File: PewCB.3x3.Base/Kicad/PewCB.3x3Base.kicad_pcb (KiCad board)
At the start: 2 copper layers, 53.3 x 53.3 mm, 4 parts

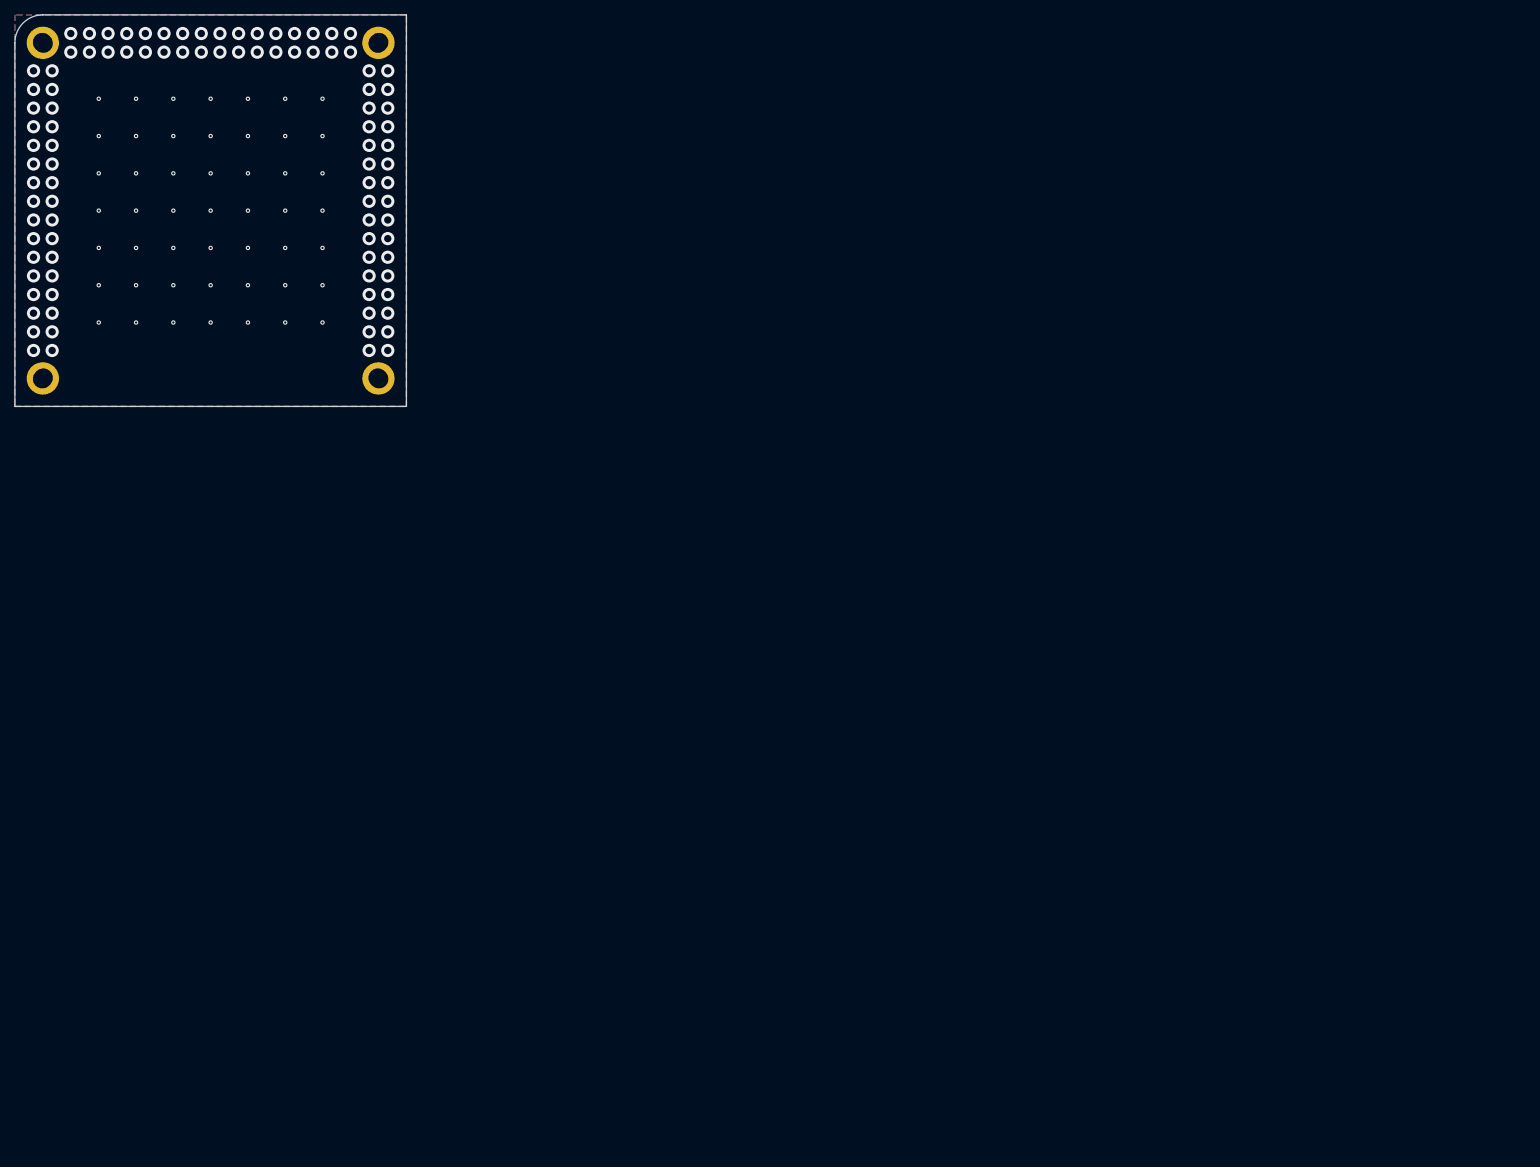
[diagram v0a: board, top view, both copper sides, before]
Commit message: fixed kicad board origins
removed empty page layouts
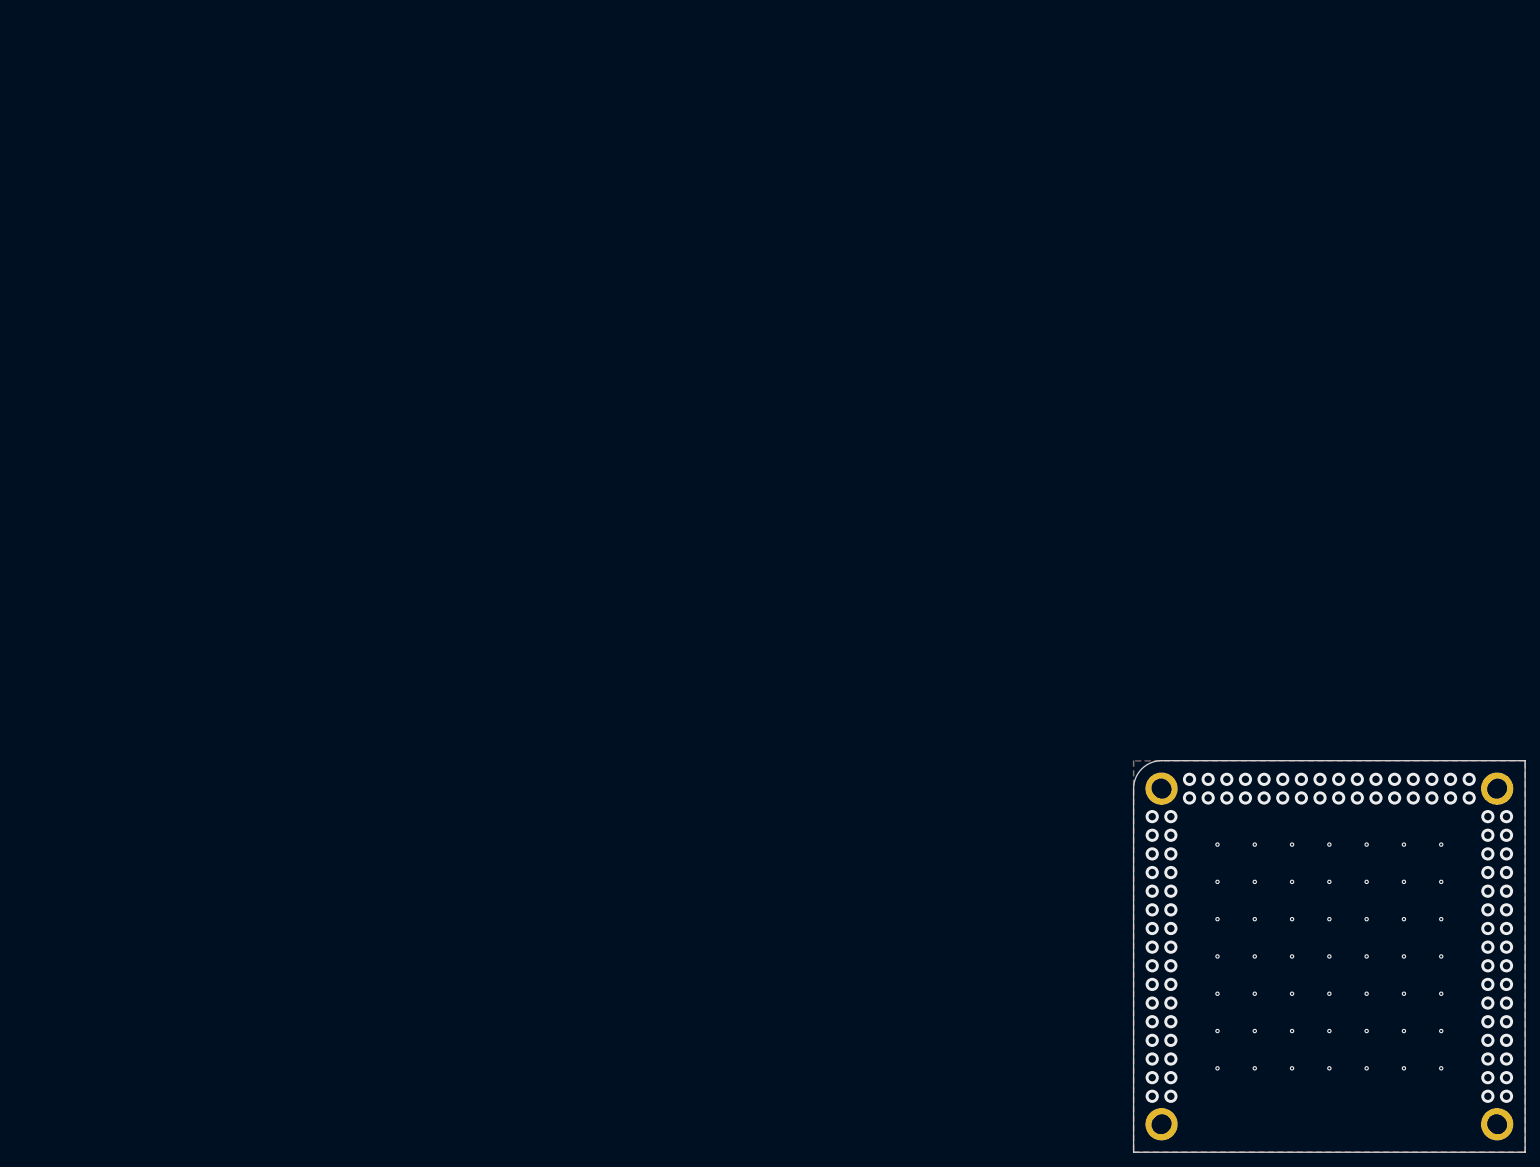
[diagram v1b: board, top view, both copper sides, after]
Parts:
- moved H** 183.2 mm to (129.5, 78.7)
- moved H** 183.2 mm to (175.3, 124.5)
- moved H** 183.2 mm to (175.3, 78.7)
- moved H** 183.2 mm to (129.5, 124.5)
